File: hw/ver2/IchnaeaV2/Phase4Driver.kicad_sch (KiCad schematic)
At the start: 21 parts, among them Q2 MCAC80N10Y, Q3 MCAC80N10Y, Q4 MCAC80N10Y, Q5 MCAC80N10Y, U2 HIP2210

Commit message: Trying to further compress power loop area
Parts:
- renumbered C6 to C24, C7 to C25, C8 to C26, C9 to C27, C10 to C28, C11 to C29, C42 to C45, C48 to C51, C54 to C57, C60 to C63, D2 to D5, L1 to L4, Q2 to Q14, Q3 to Q15, Q4 to Q16, Q5 to Q17, R4 to R16, R5 to R17, R6 to R18, R7 to R19, U2 to U5

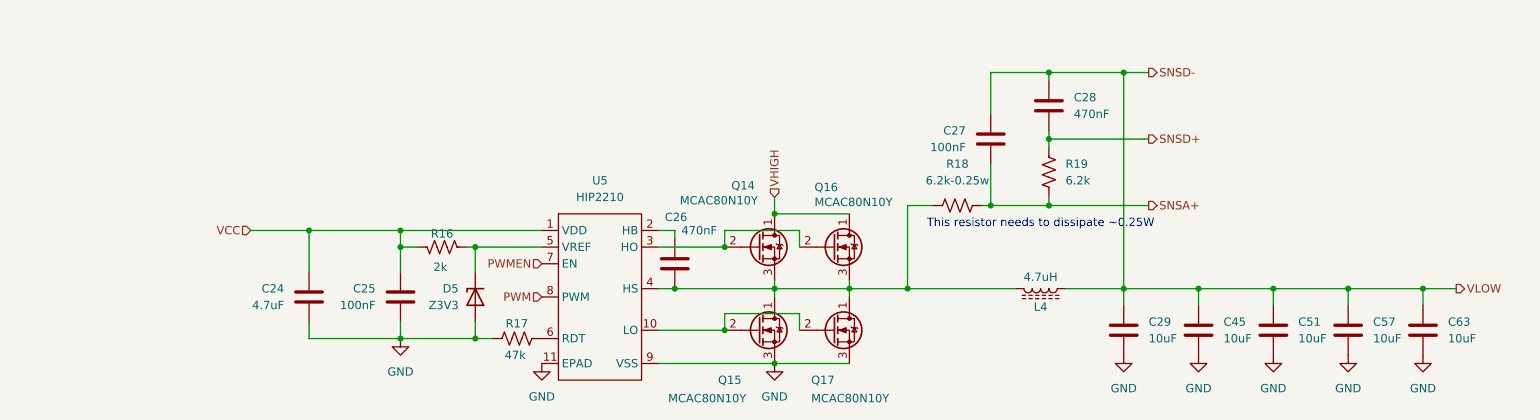
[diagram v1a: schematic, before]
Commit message: Not quite happy with the power stage just yet.
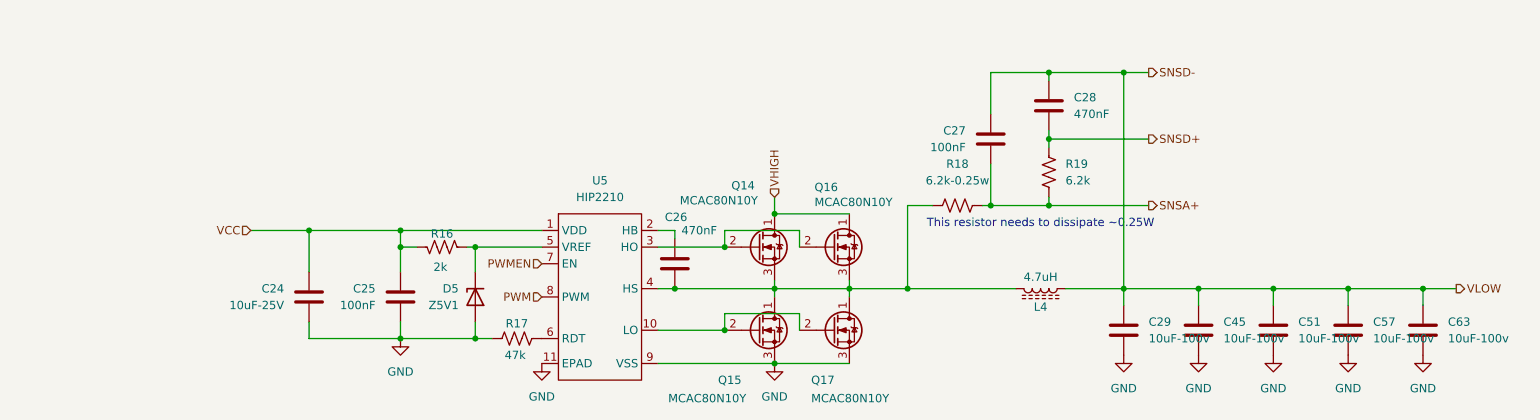
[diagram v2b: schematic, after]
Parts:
- C24: value 4.7uF -> 10uF-25V; LCSC C19666 -> C96446
- C29, C45, C51, C57, C63: value 10uF -> 10uF-100v
- D5: value Z3V3 -> Z5V1; LCSC C5353025 -> C2903912
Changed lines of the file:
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@@
 			)
 		)
-		(property "Value" "10uF"
+		(property "Value" "10uF-100v"
 			(at 242.57 102.8699 0)
 			(effects
@@
 			)
 		)
-		(property "Value" "4.7uF"
+		(property "Value" "10uF-25V"
 			(at 87.63 97.7899 0)
 			(effects
@@
 			)
 		)
-		(property "LCSC" "C19666"
+		(property "LCSC" "C96446"
 			(at 91.44 96.52 0)
 			(effects
@@
 			)
 		)
-		(property "Value" "10uF"
+		(property "Value" "10uF-100v"
 			(at 231.14 102.8699 0)
 			(effects
@@
 			)
 		)
-		(property "Value" "10uF"
+		(property "Value" "10uF-100v"
 			(at 219.71 102.8699 0)
 			(effects
@@
 			)
 		)
-		(property "Value" "Z3V3"
+		(property "Value" "Z5V1"
 			(at 114.3 97.7899 90)
 			(effects
@@
 			)
 		)
-		(property "LCSC" "C5353025"
+		(property "LCSC" "C2903912"
 			(at 116.84 96.52 90)
 			(effects
@@
 			)
 		)
-		(property "Value" "10uF"
+		(property "Value" "10uF-100v"
 			(at 254 102.8699 0)
 			(effects
@@
 			)
 		)
-		(property "Value" "10uF"
+		(property "Value" "10uF-100v"
 			(at 265.43 102.8699 0)
 			(effects

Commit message: Sync work to main PC
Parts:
- removed C25: 100nF, Capacitor_SMD:C_0603_1608Metric, symbol Device:C
- removed D5: Z5V1, Diode_SMD:D_SOD-123, symbol Device:D_Zener
- added C13, C19: 10uF-100v, Capacitor_SMD:C_1210_3225Metric_Pad1.33x2.70mm_HandSolder, symbol Device:C
- added R20: 0, Resistor_SMD:R_0603_1608Metric, symbol Device:R_US
- added R66: 10k, Resistor_SMD:R_0603_1608Metric, symbol Device:R_US
- added R67: 6.2k, Resistor_SMD:R_0603_1608Metric, symbol Device:R_US
- R16: value 2k -> 0; LCSC (none) -> C21189
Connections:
- net GND: now also C13.2, C19.2, R67.2
- net PWM: now also R20.2; no longer U5.8 (PWM)
- net PWMEN: now also R16.2; no longer U5.7 (EN)
- net SNSD-: now also L4.2; no longer L4.1
- net VCC: now also R66.1; no longer R16.2
- net VHIGH: now also C13.1, C19.1
- net at C26.2, Q14.3 (S), Q15.1 (D)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: now also L4.1; no longer L4.2
- net at R16.1: now also U5.7 (EN); no longer U5.5 (VREF)
- new net: R20.1, U5.8 (PWM)
- new net: R66.2, R67.1, U5.5 (VREF)
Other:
- moved on the sheet: C24, C26, C27, C28, C29, C45, C51, C57, C63, L4, Q14, Q15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

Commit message: More power stage layout
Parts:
- removed C29: 10uF-100v, Capacitor_SMD:C_1210_3225Metric_Pad1.33x2.70mm_HandSolder, symbol Device:C
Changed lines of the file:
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@@
-	(wire
-		(pts
-			(xy 195.58 95.25) (xy 195.58 97.79)
-		)
-		(stroke
-			(width 0)
-			(type default)
-		)
-	)
 	(wire
 		(pts
@@
 	(symbol
 		(lib_id "Device:C")
-		(at 195.58 101.6 0)
-		(unit 1)
-		(exclude_from_sim no)
-		(in_bom yes)
-		(on_board yes)
-		(dnp no)
-		(fields_autoplaced yes)
-		(property "Reference" "C29"
-			(at 199.39 100.3299 0)
-			(effects
-				(font
-					(size 1.27 1.27)
-				)
-				(justify left)
-			)
-		)
-		(property "Value" "10uF-100v"
-			(at 199.39 102.8699 0)
-			(effects
-				(font
-					(size 1.27 1.27)
-				)
-				(justify left)
-			)
-		)
-		(property "Footprint" "Capacitor_SMD:C_1210_3225Metric_Pad1.33x2.70mm_HandSolder"
-			(at 196.5452 105.41 0)
-			(effects
-				(font
-					(size 1.27 1.27)
-				)
-				(hide yes)
-			)
-		)
-		(property "Datasheet" "~"
-			(at 195.58 101.6 0)
-			(effects
-				(font
-					(size 1.27 1.27)
-				)
-				(hide yes)
-			)
-		)
-		(property "Description" "Unpolarized capacitor"
-			(at 195.58 101.6 0)
-			(effects
-				(font
-					(size 1.27 1.27)
-				)
-				(hide yes)
-			)
-		)
-		(property "Field-1" ""
-			(at 195.58 101.6 0)
-			(effects
-				(font
-					(size 1.27 1.27)
-				)
-				(hide yes)
-			)
-		)
-		(property "Digikey" "445-CGA6P1X7R1N106M250ACCT-ND"
-			(at 195.58 101.6 0)
-			(effects
-				(font
-					(size 1.27 1.27)
-				)
-				(hide yes)
-			)
-		)
-		(property "LCSC" "C576517"
-			(at 195.58 101.6 0)
-			(effects
-				(font
-					(size 1.27 1.27)
-				)
-				(hide yes)
-			)
-		)
-		(pin "1"
-		)
-		(pin "2"
-		)
-		(instances
-			(project "IchnaeaV2"
-				(path "/93408532-1ffa-463d-873c-16289d2b7987/31a930eb-86fc-490d-aa2b-31b72c4dd29d/ed7af46d-5b91-411b-a953-18bebafe1a87"
-					(reference "C29")
-					(unit 1)
-				)
-			)
-		)
-	)
-	(symbol
-		(lib_id "Device:C")
 		(at 102.87 91.44 0)
 		(unit 1)
@@
 					(unit 1)
 				)
-			)
-		)
-	)
-	(symbol
-		(lib_id "power:GND")
-		(at 195.58 105.41 0)
-		(unit 1)
-		(exclude_from_sim no)
-		(in_bom yes)
-		(on_board yes)
-		(dnp no)
-		(fields_autoplaced yes)
-		(property "Reference" "#PWR059"
-			(at 195.58 111.76 0)
-			(effects
-				(font
-					(size 1.27 1.27)
-				)
-				(hide yes)
-			)
-		)
-		(property "Value" "GND"
-			(at 195.58 110.49 0)
-			(effects
-				(font
-					(size 1.27 1.27)
-				)
-			)
-		)
-		(property "Footprint" ""
-			(at 195.58 105.41 0)
-			(effects
-				(font
-					(size 1.27 1.27)
-				)
-				(hide yes)
-			)
-		)
-		(property "Datasheet" ""
-			(at 195.58 105.41 0)
-			(effects
-				(font
-					(size 1.27 1.27)
-				)
-				(hide yes)
-			)
-		)
-		(property "Description" "Power symbol creates a global label with name \"GND\" , ground"
-			(at 195.58 105.41 0)
-			(effects
-				(font
-					(size 1.27 1.27)
-				)
-				(hide yes)
-			)
-		)
-		(pin "1"
-		)
-		(instances
-			(project "IchnaeaV2"
-				(path "/93408532-1ffa-463d-873c-16289d2b7987/31a930eb-86fc-490d-aa2b-31b72c4dd29d/ed7af46d-5b91-411b-a953-18bebafe1a87"
-					(reference "#PWR059")
-					(unit 1)
-				)

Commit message: Partially work through the V1 notes. Start adding some of the control stage circuitry.
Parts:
- added TP27, TP28, TP29, TP30, TP31, TP46, TP47, TP48: TestPoint, TestPoint:TestPoint_Pad_D1.0mm, symbol Connector:TestPoint
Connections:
- net GND: now also TP29.1, TP46.1
- net PWM: now also TP31.1
- net PWMEN: now also TP30.1
- net SNSD-: now also TP48.1
- net at C26.2, L4.1, Q14.3 (S)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: now also TP47.1
- net at Q15.2 (G), Q17.2 (G), U5.10 (LO): now also TP28.1
- net at Q14.2 (G), Q16.2 (G), U5.3 (HO): now also TP27.1
